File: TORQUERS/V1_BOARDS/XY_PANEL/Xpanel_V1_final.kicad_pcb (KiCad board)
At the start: 4 copper layers, 82.6 x 98 mm, 64 parts, among them J2 F3311A7H121014E200, Q1 BSS138, Q10 BSS138, Q11 BSS138, Q12 MBT2222ADW1T1, Q13 BSS138, Q14 BSS138, Q15 MBT2222ADW1T1, Q2 BSS138, Q3 MBT2222ADW1T1, Q4 BSS138, Q5 BSS138, Q6 MBT2222ADW1T1, U1 DRV8830DGQ, U2 OPT4001DTST, U3 LTC3130EUDC-1-PBF

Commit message: Made changes to LTC ; remaining switches for H bridge and  LTC3130 for 70mm panel
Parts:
- moved S2 271.3 mm to (181.1, 121.6), turned to 180 degrees
- moved S1 261.8 mm to (187.4, 51.3), turned to -90 degrees
- moved S4 199.7 mm to (124.3, 93.2)
- moved S3 190.6 mm to (116.1, 82.9), turned to 90 degrees
- moved C5 98.0 mm to (58.1, 90.8)
- moved C6 98.0 mm to (58.1, 93.3)
- moved D1 98.0 mm to (70.6, 91.9)
- moved D4 98.0 mm to (70.6, 96.5)
- moved Q12 98.0 mm to (75.2, 91.5)
- moved Q15 98.0 mm to (75.2, 95.4)
- moved R19 98.0 mm to (58.1, 95.9)
- moved R20 98.0 mm to (58.1, 98.4)
- moved R21 98.0 mm to (62.1, 90.8)
- moved R23 98.0 mm to (62.1, 93.3)
- moved R24 98.0 mm to (62.1, 95.9)
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
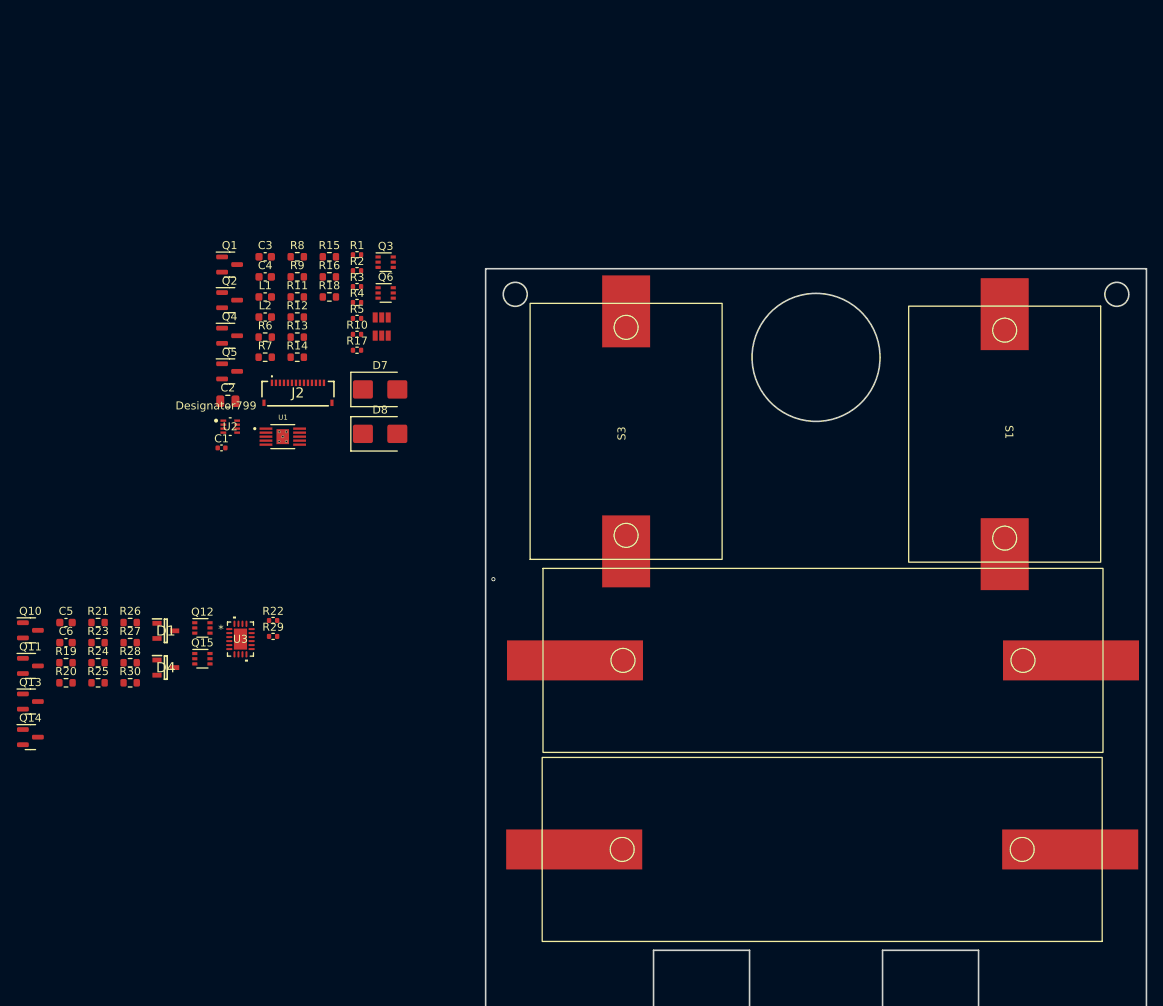
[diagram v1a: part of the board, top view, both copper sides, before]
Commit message: Schematic lock on XY BOARD
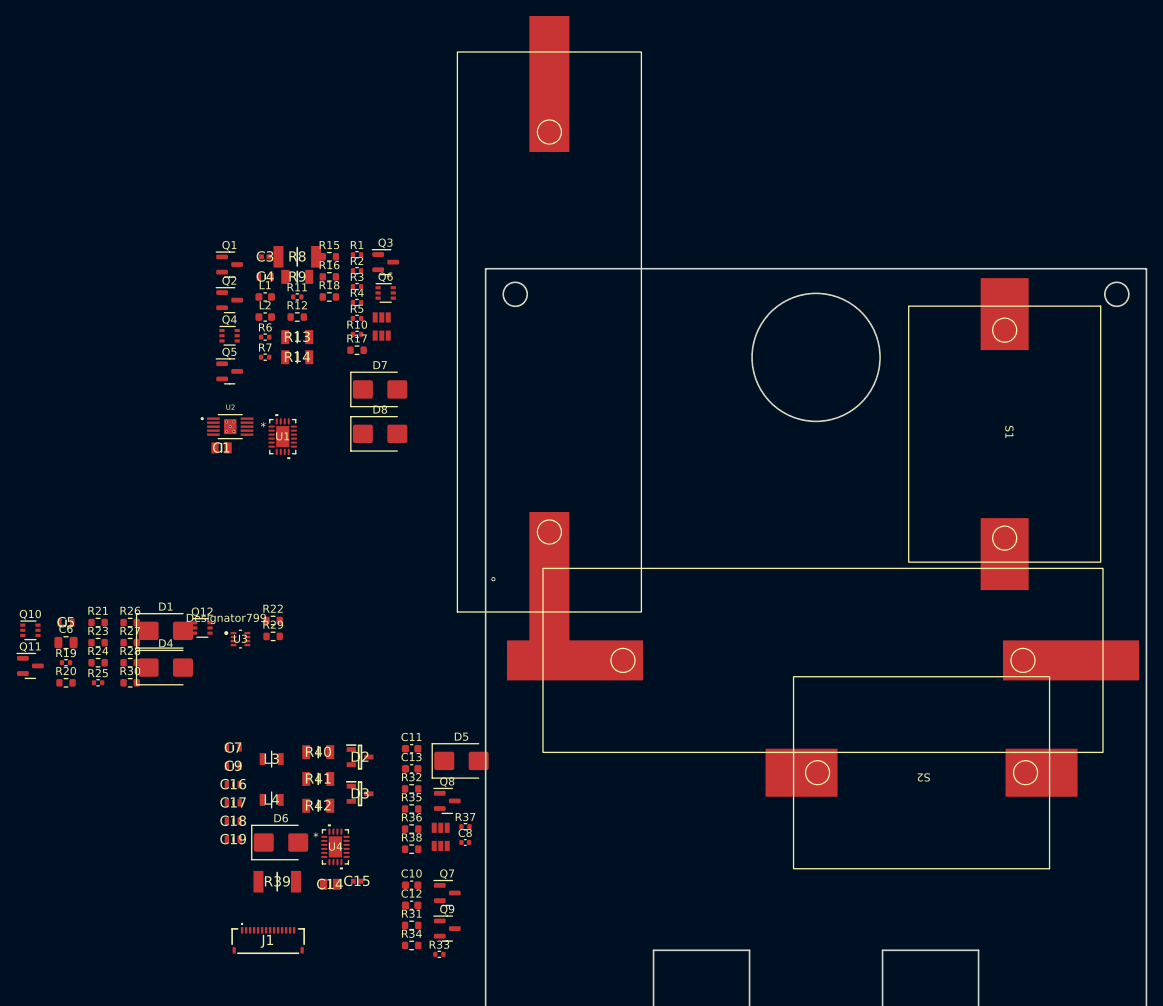
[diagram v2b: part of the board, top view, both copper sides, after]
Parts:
- removed C2: 10uF, Capacitor_SMD:C_0805_2012Metric
- removed J2: F3311A7H121014E200, F3311A7H121008E200:F3311A7H121014E200
- removed Q13, Q14: BSS138, Package_TO_SOT_SMD:SOT-23
- removed Q15: MBT2222ADW1T1, Package_TO_SOT_SMD:SOT-363_SC-70-6
- added C10: 10nF, Capacitor_SMD:C_0603_1608Metric, F.Cu at (101.3, 123.7)
- added C11: 10nF, Capacitor_SMD:C_0603_1608Metric, F.Cu at (101.3, 106.6)
- added C12: 10nF, Capacitor_SMD:C_0603_1608Metric, F.Cu at (101.3, 126.2)
- added C13: 10nF, Capacitor_SMD:C_0603_1608Metric, F.Cu at (101.3, 109.1)
- added C14: CL21A476MQYNNNE, AA_AUTO_LOADER:CAPC2012X135N, F.Cu at (91.1, 123.6)
- added C15: CL05A105KQ5NNNC, AA_AUTO_LOADER:CAPC1005X55N, F.Cu at (94.5, 123.2)
- added C16: CL10A475KQ8NNNC, AA_AUTO_LOADER:CAPC1608X90N, F.Cu at (79.0, 111.1)
- added C17: CGA3E2X7R1H223K080AA, AA_AUTO_LOADER:CAPC1608X90N, F.Cu at (79.0, 113.4)
- added C18: CGA3E2X7R1H223K080AA, AA_AUTO_LOADER:CAPC1608X90N, F.Cu at (79.0, 115.7)
- added C19: CL10A475KQ8NNNC, AA_AUTO_LOADER:CAPC1608X90N, F.Cu at (79.0, 118.0)
- added C7: CGA3E2X7R1H223K080AA, AA_AUTO_LOADER:CAPC1608X90N, F.Cu at (79.0, 106.5)
- added C8: 0.1uF, Capacitor_SMD:C_0402_1005Metric, F.Cu at (108.0, 118.3)
- added C9: CL10A475KQ8NNNC, AA_AUTO_LOADER:CAPC1608X90N, F.Cu at (79.0, 108.8)
- added D2: BAV99-TP, AA_AUTO_LOADER:SOT95P237X125-3N, F.Cu at (94.9, 107.7)
- added D3: BAV99-TP, AA_AUTO_LOADER:SOT95P237X125-3N, F.Cu at (94.9, 112.2)
- added D5: B220, Diode_SMD:D_SMB, F.Cu at (107.5, 108.1)
- added D6: B220, Diode_SMD:D_SMB, F.Cu at (85.0, 118.3)
- added J1: F3311A7H121014E200, F3311A7H121008E200:F3311A7H121014E200, F.Cu at (83.4, 130.7)
- added JP3: ~, SparkFun-Jumper:SMT-JUMPER_3_NO_NO-SILK, F.Cu at (105.0, 116.5)
- added JP4: ~, SparkFun-Jumper:SMT-JUMPER_3_NO_NO-SILK, F.Cu at (105.0, 118.8)
- added L3: LQM2HPN4R7MG0L, AA_AUTO_LOADER:LQM2HPN1R0MG0L, F.Cu at (83.8, 107.9)
- added L4: LQM2HPN4R7MG0L, AA_AUTO_LOADER:LQM2HPN1R0MG0L, F.Cu at (83.8, 113.0)
- added Q7: BSS138, Package_TO_SOT_SMD:SOT-23, F.Cu at (105.8, 124.6)
- added Q8: BSS138, Package_TO_SOT_SMD:SOT-23, F.Cu at (105.8, 113.1)
- added Q9: BSS138, Package_TO_SOT_SMD:SOT-23, F.Cu at (105.8, 129.1)
- added R31: 10K, Resistor_SMD:R_0603_1608Metric, F.Cu at (101.3, 128.7)
- added R32: 10K, Resistor_SMD:R_0603_1608Metric, F.Cu at (101.3, 111.6)
- added R33: 10K, Resistor_SMD:R_0402_1005Metric, F.Cu at (104.8, 132.3)
- added R34: 100K, Resistor_SMD:R_0603_1608Metric, F.Cu at (101.3, 131.2)
- added R35: 600, Resistor_SMD:R_0603_1608Metric, F.Cu at (101.3, 114.1)
- added R36: 10K, Resistor_SMD:R_0603_1608Metric, F.Cu at (101.3, 116.7)
- added R37: 10K, Resistor_SMD:R_0402_1005Metric, F.Cu at (108.0, 116.4)
- added R38: 100K, Resistor_SMD:R_0603_1608Metric, F.Cu at (101.3, 119.2)
- added R39: CHV2010-FX-1005ELF, AA_AUTO_LOADER:RESC5025X70N, F.Cu at (84.5, 123.2)
- added R40: RC1206FR-072M49L, AA_AUTO_LOADER:RESC3116X65N, F.Cu at (89.6, 107.0)
- added R41: RV1206JR-0722ML, AA_AUTO_LOADER:RESC3116X65N, F.Cu at (89.6, 110.4)
- added R42: RC1206FR-072ML, AA_AUTO_LOADER:RESC3116X65N, F.Cu at (89.6, 113.7)
- added U4: LTC3130EUDC-1-PBF, LTC3130:UDC_20_ADI, F.Cu at (91.8, 118.9)
- C1: value 0.1uF -> CL21A476MQYNNNE; footprint Capacitor_SMD:C_0402_1005Metric -> AA_AUTO_LOADER:CAPC2012X135N
- C3: value 10nF -> CL05A105KQ5NNNC; footprint Capacitor_SMD:C_0603_1608Metric -> AA_AUTO_LOADER:CAPC1005X55N
- C4: value 10nF -> CL10A475KQ8NNNC; footprint Capacitor_SMD:C_0603_1608Metric -> AA_AUTO_LOADER:CAPC1608X90N
- C5: value 10nF -> CGA3E2X7R1H223K080AA; footprint Capacitor_SMD:C_0603_1608Metric -> AA_AUTO_LOADER:CAPC1608X90N
- C6: value 10nF -> 10uF; footprint Capacitor_SMD:C_0603_1608Metric -> Capacitor_SMD:C_0805_2012Metric
- D1, D4: value BAV99-TP -> B220; footprint AA_AUTO_LOADER:SOT95P237X125-3N -> Diode_SMD:D_SMB
- Q10, Q4: value BSS138 -> MBT2222ADW1T1; footprint Package_TO_SOT_SMD:SOT-23 -> Package_TO_SOT_SMD:SOT-363_SC-70-6
- Q3: value MBT2222ADW1T1 -> BSS138; footprint Package_TO_SOT_SMD:SOT-363_SC-70-6 -> Package_TO_SOT_SMD:SOT-23
- R10, R28: value 10K -> 0
- R11: value 100K -> 0; footprint Resistor_SMD:R_0603_1608Metric -> Resistor_SMD:R_0402_1005Metric
- R13: value 0 -> RV1206JR-0722ML; footprint Resistor_SMD:R_0603_1608Metric -> AA_AUTO_LOADER:RESC3116X65N
- R14, R9: value 10K -> RC1206FR-072ML; footprint Resistor_SMD:R_0603_1608Metric -> AA_AUTO_LOADER:RESC3116X65N
- R15: value 600 -> 10K
- R16, R21: value 10K -> 600
- R17, R29: footprint Resistor_SMD:R_0402_1005Metric -> Resistor_SMD:R_0603_1608Metric
- R18: value 100K -> 10K
- R19, R6: footprint Resistor_SMD:R_0603_1608Metric -> Resistor_SMD:R_0402_1005Metric
- R20: value 600 -> 100K
- R22: value 10K -> 0; footprint Resistor_SMD:R_0402_1005Metric -> Resistor_SMD:R_0603_1608Metric
- R23: value 100K -> 0
- R24: value 0 -> 10K
- R25: value 0 -> 10K; footprint Resistor_SMD:R_0603_1608Metric -> Resistor_SMD:R_0402_1005Metric
- R26: value 10K -> 100K
- R27: value 600 -> 0
- R30: value 100K -> 600
- R7: value 10K -> 0; footprint Resistor_SMD:R_0603_1608Metric -> Resistor_SMD:R_0402_1005Metric
- R8: value 600 -> CHV2010-FX-1005ELF; footprint Resistor_SMD:R_0603_1608Metric -> AA_AUTO_LOADER:RESC5025X70N
- S2: value sol_pan_70x23 -> sol_pan_32x24; footprint CUSTOM_SOLAR_7023:sol_pan_SM141K10TFS_70x23 -> CUSTOM_SOLAR_2432:solar_panel_SM500K12TF_32x24
- S3: value sol_pan_32x24 -> sol_pan_70x23; footprint CUSTOM_SOLAR_2432:solar_panel_SM500K12TF_32x24 -> CUSTOM_SOLAR_7023:sol_pan_SM141K10TFS_70x23
- U1: value DRV8830DGQ -> LTC3130EUDC-1-PBF; footprint DRV8830DGQ:IC_XTR111AIDGQR -> LTC3130:UDC_20_ADI
- U2: value OPT4001DTST -> DRV8830DGQ; footprint OPT4001DTST:DTS0008A-MFG -> DRV8830DGQ:IC_XTR111AIDGQR
- U3: value LTC3130EUDC-1-PBF -> OPT4001DTST; footprint LTC3130:UDC_20_ADI -> OPT4001DTST:DTS0008A-MFG
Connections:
- net /3224_vout renamed /solar_panel_electronics/3224_vout
- C1 pad 1: Net-(D7-K) -> GND
- C1 pad 2: GND -> Net-(D1-K)
- C3 pad 1: Net-(Q2-G) -> GND
- C3 pad 2: GND -> Net-(U1-RUN)
- C4 pad 1: Net-(Q5-G) -> GND
- C4 pad 2: GND -> Net-(U1-VCC)
- C5 pad 1: Net-(Q11-G) -> Net-(U1-SW1)
- C5 pad 2: GND -> Net-(U1-BST1)
- C6 pad 1: Net-(Q14-G) -> Net-(D4-K)
- D1 pad 1: GND -> Net-(D1-K)
- D4 pad 1: GND -> Net-(D4-K)
- D4 pad 2: /7023_vout -> +3.3V
- D7 pad 1: Net-(D7-K) -> VSOLAR
- D7 pad 2: +3.3V -> Net-(D7-A)
- D8 pad 1: Net-(D7-K) -> VSOLAR
- D8 pad 2: VBATT -> Net-(D8-A)
- JP2 pad 3: /+3.3v -> /SUN_SENSOR/+3.3v
- L1 pad 1: /coils -> Net-(JP3-B)
- L1 pad 2: Net-(U1-OUT1) -> Net-(U2-OUT1)
- L2 pad 1: /coils -> Net-(JP3-A)
- L2 pad 2: Net-(U1-OUT2) -> Net-(U2-OUT2)
- Q10 pad 1: Net-(Q10-G) -> SDA1_b4iso
- Q10 pad 2: Net-(Q10-S) -> Net-(Q10A-B1)
- Q10 pad 3: GND -> SDA1_b4iso
- Q11 pad 2: Net-(Q10-G) -> Net-(Q11-S)
- Q12 pad 1: SCL1_b4iso -> SDA1_b4iso
- Q12 pad 3: SCL1_b4iso -> SDA1_b4iso
- Q12 pad 4: SCL_SUN -> SDA_TORQUE
- Q12 pad 5: Net-(Q10-S) -> Net-(Q12B-B2)
- Q12 pad 6: SCL_SUN -> SDA_TORQUE
- Q2 pad 2: Net-(Q1-G) -> Net-(Q2-S)
- Q3 pad 1: SCL1_b4iso -> Net-(Q3-G)
- Q3 pad 2: Net-(Q3A-B1) -> Net-(Q1-G)
- Q3 pad 3: SCL1_b4iso -> GND
- Q4 pad 1: Net-(Q4-G) -> SCL1_b4iso
- Q4 pad 2: Net-(Q4-S) -> Net-(Q4A-B1)
- Q4 pad 3: GND -> SCL1_b4iso
- Q5 pad 2: Net-(Q4-G) -> Net-(Q2-G)
- Q6 pad 1: SDA1_b4iso -> SCL1_b4iso
- Q6 pad 3: SDA1_b4iso -> SCL1_b4iso
- Q6 pad 4: SDA_TORQUE -> SCL_TORQUE
- Q6 pad 5: Net-(Q4-S) -> Net-(Q2-S)
- Q6 pad 6: SDA_TORQUE -> SCL_TORQUE
- R1 pad 1: Net-(U1-A0) -> Net-(U2-ISENSE)
- R1 pad 2: +3.3V -> GND
- R10 pad 1: SCL_TORQUE -> Net-(U2-A1)
- R11 pad 1: Net-(Q2-G) -> GND
- R11 pad 2: SCL_TORQUE -> Net-(U2-A1)
- R12 pad 1: SCL1_b4iso -> +3.3V
- R12 pad 2: SCL_TORQUE -> Net-(D4-K)
- R13 pad 1: SDA1_b4iso -> /solar_panel_electronics/FB
- R13 pad 2: SDA_TORQUE -> Net-(D8-A)
- R14 pad 1: Net-(Q4-G) -> GND
- R14 pad 2: +3.3V -> /solar_panel_electronics/FB
- R15 pad 1: Net-(Q6A-B1) -> Net-(Q1-G)
- R15 pad 2: Net-(Q4-S) -> +3.3V
- R16 pad 1: +3.3V -> Net-(Q1-S)
- R16 pad 2: Net-(Q4-S) -> Net-(Q4A-B1)
- R17 pad 1: SDA_TORQUE -> +3.3V
- R17 pad 2: +3.3V -> Net-(Q1-S)
- R18 pad 1: Net-(Q5-G) -> Net-(Q2-G)
- R18 pad 2: SDA_TORQUE -> +3.3V
- R19 pad 1: Net-(Q10-G) -> SCL_SUN
- R2 pad 1: GND -> Net-(U2-ISENSE)
- R2 pad 2: Net-(U1-A0) -> GND
- R20 pad 1: Net-(Q10-S) -> Net-(Q3-G)
- R20 pad 2: Net-(Q12A-B1) -> SCL_SUN
- R21 pad 1: +3.3V -> Net-(Q2-S)
- R21 pad 2: Net-(Q10-S) -> Net-(Q6A-B1)
- R22 pad 1: SCL_SUN -> SCL1_b4iso
- R22 pad 2: +3.3V -> SCL_SUN
- R23 pad 1: Net-(Q11-G) -> SDA1_b4iso
- R23 pad 2: SCL_SUN -> SDA_SUN
- R24 pad 1: SCL1_b4iso -> +3.3V
- R24 pad 2: SCL_SUN -> Net-(Q2-S)
- R25 pad 1: SDA1_b4iso -> SCL_TORQUE
- R25 pad 2: SDA_SUN -> +3.3V
- R26 pad 1: Net-(Q13-G) -> Net-(Q5-G)
- R26 pad 2: +3.3V -> SCL_TORQUE
- R27 pad 1: Net-(Q15A-B1) -> SCL1_b4iso
- R27 pad 2: Net-(Q13-S) -> SCL_TORQUE
- R28 pad 1: +3.3V -> SDA1_b4iso
- R28 pad 2: Net-(Q13-S) -> SDA_TORQUE
- R29 pad 1: SDA_SUN -> Net-(Q7-G)
- R3 pad 1: Net-(U1-A1) -> Net-(U2-ISENSE)
- R3 pad 2: +3.3V -> GND
- R30 pad 1: Net-(Q14-G) -> Net-(Q10A-B1)
- R30 pad 2: SDA_SUN -> Net-(Q10B-B2)
- R4 pad 1: GND -> Net-(U2-ISENSE)
- R4 pad 2: Net-(U1-A1) -> GND
- R5 pad 1: Net-(U1-ISENSE) -> Net-(U2-ISENSE)
- R6 pad 1: +3.3V -> GND
- R6 pad 2: Net-(D7-K) -> Net-(U2-A0)
- R7 pad 1: Net-(Q1-G) -> Net-(U2-A0)
- R8 pad 1: Net-(Q1-S) -> /solar_panel_electronics/MPPC
- R8 pad 2: Net-(Q3A-B1) -> Net-(D1-K)
- R9 pad 1: +3.3V -> GND
- R9 pad 2: Net-(Q1-S) -> /solar_panel_electronics/MPPC
- S1 pad 2: Net-(D1-K/A) -> Net-(D2-K/A)
- S2 pad 1: /7023_vout -> Net-(D2-K/A)
- S2 pad 2: Net-(D4-K/A) -> GND
- S3 pad 1: Net-(D1-K/A) -> /solar_panel_electronics/7023_vout
- S3 pad 2: GND -> Net-(D3-K/A)
- S4 pad 1: Net-(D4-K/A) -> Net-(D3-K/A)
- U1 pad 1: Net-(U1-OUT2) -> Net-(U1-BST1)
- U1 pad 10: SCL_TORQUE -> Net-(U1-VCC)
- U1 pad 12: (no net) -> Net-(U1-EXTVCC)
- U1 pad 13: (no net) -> unconnected-(U1-PGOOD-Pad13)
- U1 pad 14: (no net) -> Net-(D8-A)
- U1 pad 15: (no net) -> Net-(U1-SW2)
- U1 pad 16: (no net) -> Net-(U1-BST2)
- U1 pad 2: Net-(U1-ISENSE) -> Net-(D1-K)
- U1 pad 3: Net-(U1-OUT1) -> Net-(U1-RUN)
- U1 pad 4: Net-(D7-K) -> Net-(U1-RUN)
- U1 pad 5: GND -> Net-(U1-VCC)
- U1 pad 6: unconnected-(U1-FAULTN-Pad6) -> /solar_panel_electronics/MPPC
- U1 pad 7: Net-(U1-A0) -> GND
- U1 pad 8: Net-(U1-A1) -> GND
- U1 pad 9: SDA_TORQUE -> /solar_panel_electronics/FB
- U2 pad 1: /+3.3v -> Net-(U2-OUT2)
- U2 pad 2: Net-(JP1-C) -> Net-(U2-ISENSE)
- U2 pad 3: unconnected-(U2-NC-Pad3) -> Net-(U2-OUT1)
- U2 pad 4: GND -> Net-(D4-K)
- U2 pad 5: SCL_SUN -> GND
- U2 pad 7: unconnected-(U2-INT-Pad7) -> Net-(U2-A0)
- U2 pad 8: SDA_SUN -> Net-(U2-A1)
- U3 pad 1: unconnected-(U3-BST1-Pad1) -> /SUN_SENSOR/+3.3v
- U3 pad 2: unconnected-(U3-PVIN-Pad2) -> Net-(JP1-C)
- U3 pad 4: unconnected-(U3-RUN-Pad4) -> GND
- U3 pad 5: unconnected-(U3-VCC-Pad5) -> SCL_SUN
- U3 pad 8: unconnected-(U3-GND-Pad8) -> SDA_SUN
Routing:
- net Net-(JP3-A): track 0.00 -> 34633.5 mm, vias 0 -> 1
- net /coils: track 34633.5 -> 0.00 mm, vias 1 -> 0

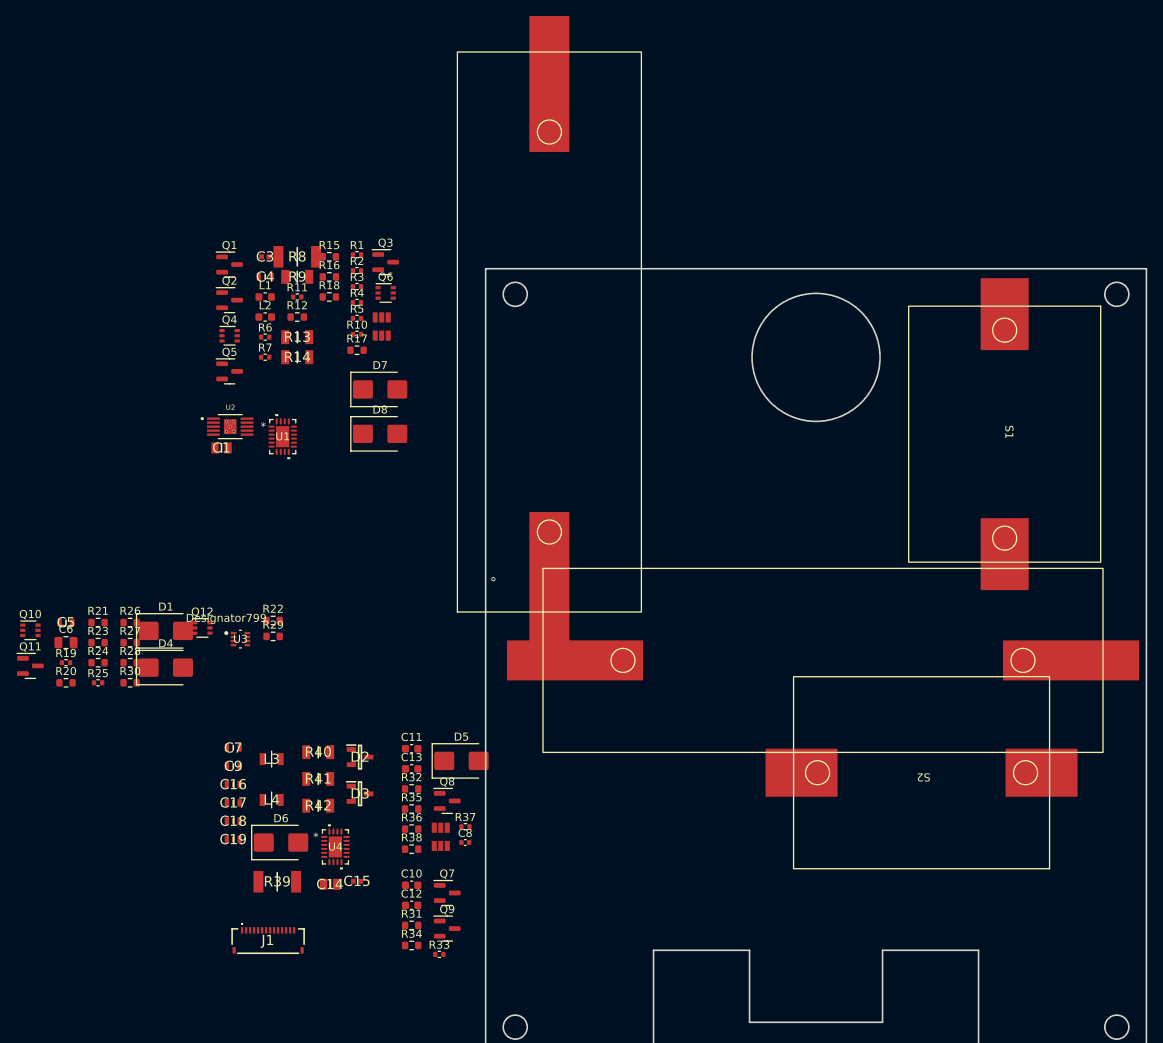
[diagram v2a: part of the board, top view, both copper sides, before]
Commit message: completed XY Board
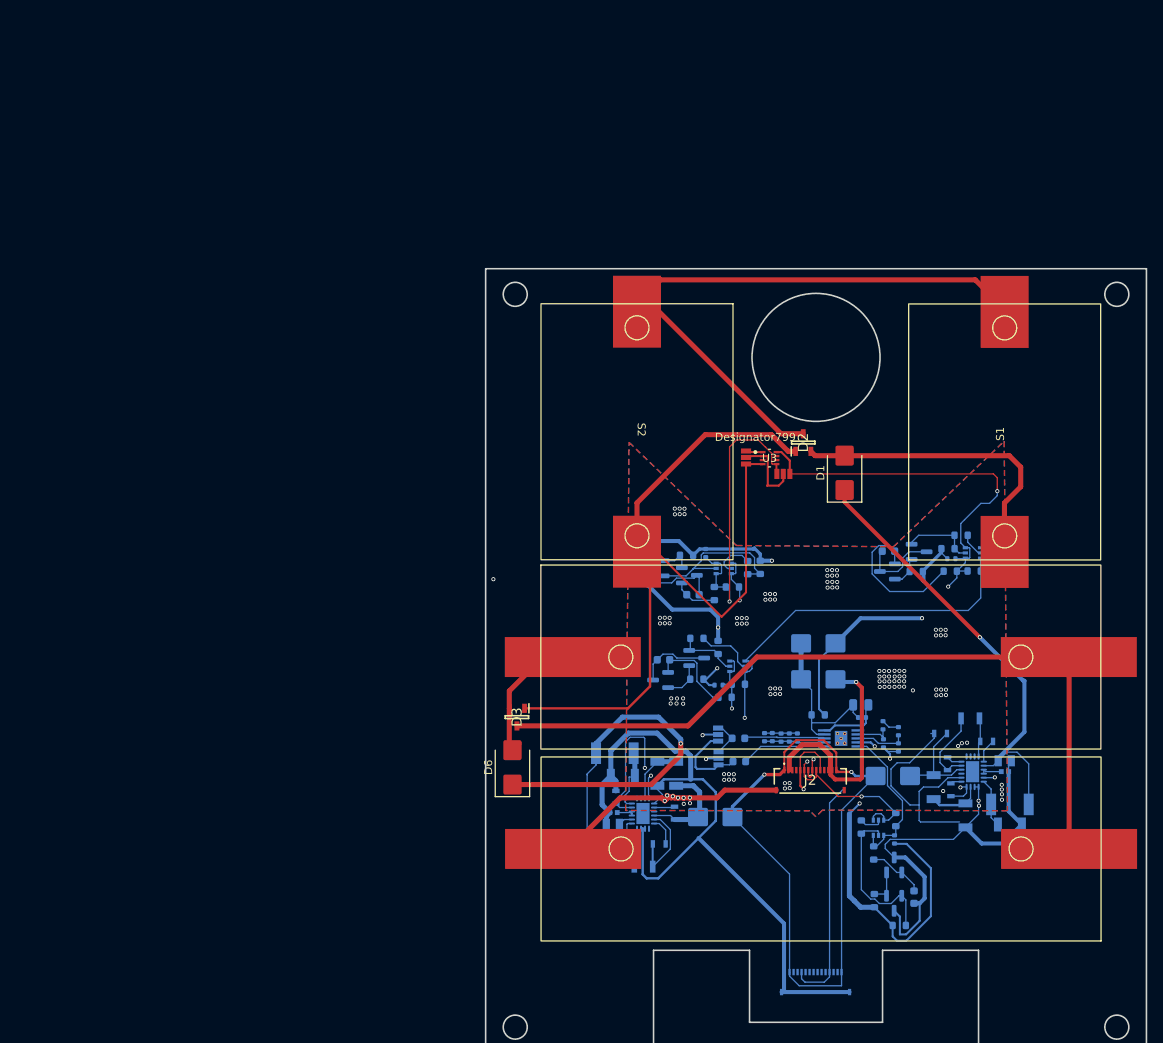
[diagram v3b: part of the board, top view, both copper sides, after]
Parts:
- added J2: F3311A7H121014E200, F3311A7H121008E200:F3311A7H121014E200, F.Cu at (151.2, 110.6)
- C1, C10, C11, C12, C13, C14, C15, C16, C17, C18, C19, C3, C4, C5, C6, C7, C8, C9, D4, D5, D7, D8, J1, JP3, JP4, L1, L2, L3, L4, Q1, Q10, Q11, Q12, Q2, Q3, Q4, Q5, Q6, Q7, Q8, Q9, R1, R10, R11, R12, R13, R14, R15, R16, R17, R18, R19, R2, R20, R21, R22, R23, R24, R25, R26, R27, R28, R29, R3, R30, R31, R32, R33, R34, R35, R36, R37, R38, R39, R4, R40, R41, R42, R5, R6, R7, R8, R9, U1, U2, U4: moved to B.Cu
- moved Q10 118.2 mm to (171.5, 82.1), turned to 180 degrees
- moved C5 116.0 mm to (173.2, 105.7)
- moved C3 112.7 mm to (175.5, 109.5), turned to 180 degrees
- moved R8 112.3 mm to (176.1, 113.6)
- moved R9 112.3 mm to (176.1, 116.1), turned to 180 degrees
- moved Q2 112.2 mm to (161.6, 125.9), turned to -90 degrees
- moved R23 109.9 mm to (171.6, 84.4), turned to 180 degrees
- moved C4 107.0 mm to (168.7, 111.7), turned to -90 degrees
- moved R30 105.5 mm to (170.0, 79.9), turned to 180 degrees
- moved C1 105.4 mm to (175.5, 108.1), turned to 180 degrees
- moved R24 105.4 mm to (162.3, 128.7)
- moved Q5 103.5 mm to (161.6, 121.1), turned to 90 degrees
- moved R18 101.7 mm to (159.2, 125.6), turned to -90 degrees
- moved R25 101.5 mm to (161.7, 118.0), turned to -90 degrees
- moved R14 101.3 mm to (170.5, 114.9), turned to 90 degrees
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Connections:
- net /TORQUE_COIL/coils renamed coils
- J1 pad 10: +3.3V -> unconnected-(J1-Pad10)
- J1 pad 12: VBATT -> unconnected-(J1-Pad12)
- J1 pad 13: VBATT -> unconnected-(J1-Pad13)
- J1 pad 2: VBATT -> unconnected-(J1-Pad2)
- J1 pad 3: VBATT -> unconnected-(J1-Pad3)
- J1 pad 5: +3.3V -> unconnected-(J1-Pad5)
- J1 pad 6: SCL1_b4iso -> unconnected-(J1-Pad6)
- J1 pad 7: SDA1_b4iso -> unconnected-(J1-Pad7)
- J1 pad 8: SDA1_b4iso -> unconnected-(J1-Pad8)
- J1 pad 9: SCL1_b4iso -> unconnected-(J1-Pad9)
- R39 pad 1: /solar_panel_electronics/MPPC -> /solar_panel_electronics/MPPC1
- R40 pad 2: /solar_panel_electronics/MPPC -> /solar_panel_electronics/MPPC1
- R41 pad 1: /solar_panel_electronics/FB -> /solar_panel_electronics/FB1
- R42 pad 2: /solar_panel_electronics/FB -> /solar_panel_electronics/FB1
- U4 pad 6: /solar_panel_electronics/MPPC -> /solar_panel_electronics/MPPC1
- U4 pad 9: /solar_panel_electronics/FB -> /solar_panel_electronics/FB1
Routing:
- net coils: track 0.00 -> 34691.2 mm, vias 0 -> 3
- net Net-(JP3-A): track 34633.5 -> 10.1 mm, vias 1 -> 0
- net GND: track 0.00 -> 352.6 mm, vias 0 -> 113
- net +3.3V: track 0.00 -> 186.7 mm, vias 0 -> 8
- net Net-(D3-K/A): track 0.00 -> 96.6 mm
- net VSOLAR: track 0.00 -> 84.9 mm, vias 0 -> 2
- net Net-(D2-K/A): track 0.00 -> 76.6 mm
- net SDA1_b4iso: track 0.00 -> 62.7 mm, vias 0 -> 2
- net Net-(D6-K): track 0.00 -> 57.3 mm, vias 0 -> 1
- net Net-(D1-K): track 0.00 -> 56.6 mm, vias 0 -> 1
- net SCL1_b4iso: track 0.00 -> 51.3 mm, vias 0 -> 3
- net SDA_SUN: track 0.00 -> 50.8 mm, vias 0 -> 2
- net SCL_SUN: track 0.00 -> 38.2 mm, vias 0 -> 1
- net /solar_panel_electronics/3224_vout: track 0.00 -> 38.1 mm
- net VBATT: track 0.00 -> 30.9 mm, vias 0 -> 1
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- added copper zone on B.Cu, net GND
- added copper zone on F.Cu, net GND
- added copper zone on In1.Cu, net GND
- added copper zone on In2.Cu, net GND
